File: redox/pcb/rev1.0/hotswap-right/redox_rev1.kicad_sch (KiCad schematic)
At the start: 75 parts, among them K0 KEYSW, K1 KEYSW, K10 KEYSW, K11 KEYSW, K12 KEYSW, K13 KEYSW, K14 KEYSW, K15 KEYSW, K16 KEYSW, K2 KEYSW, K20 KEYSW, K21 KEYSW, K22 KEYSW, K23 KEYSW, K24 KEYSW, K25 KEYSW, K26 KEYSW, K3 KEYSW, K30 KEYSW, K31 KEYSW, K32 KEYSW, K33 KEYSW, K34 KEYSW, K35 KEYSW, K36 KEYSW, K4 KEYSW, K40 KEYSW, K41 KEYSW, K42 KEYSW, K43 KEYSW, K44 KEYSW, K45 KEYSW, K46 KEYSW, K5 KEYSW, K6 KEYSW, U1 ProMicro

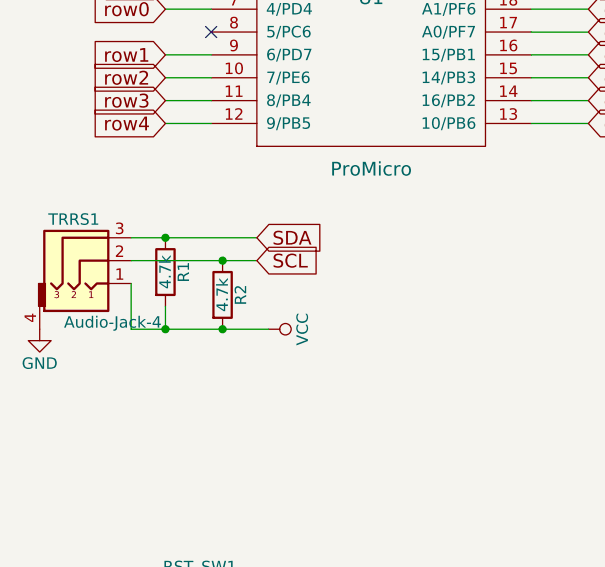
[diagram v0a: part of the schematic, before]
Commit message: Remove pullup resistors from right schematic
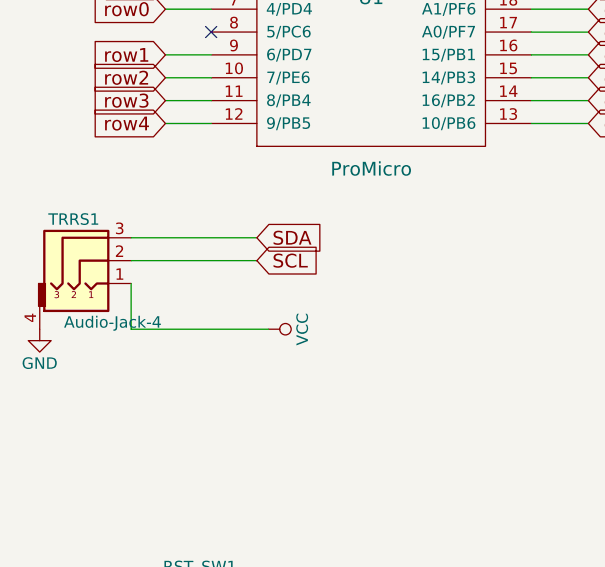
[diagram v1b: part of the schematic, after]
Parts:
- removed R1, R2: 4.7k, redox_footprints:Resistor-Compact, symbol redox_rev1-rescue:R
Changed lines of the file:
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@@
   (junction (at 177.8 48.26) (diameter 0) (color 0 0 0 0)
   )
-  (junction (at 43.18 83.82) (diameter 0) (color 0 0 0 0)
-  )
   (junction (at 233.68 57.15) (diameter 0) (color 0 0 0 0)
   )
@@
   (junction (at 152.4 74.93) (diameter 0) (color 0 0 0 0)
   )
-  (junction (at 36.83 91.44) (diameter 0) (color 0 0 0 0)
-  )
   (junction (at 157.48 124.46) (diameter 0) (color 0 0 0 0)
   )
@@
   (junction (at 137.16 124.46) (diameter 0) (color 0 0 0 0)
   )
-  (junction (at 36.83 81.28) (diameter 0) (color 0 0 0 0)
-  )
   (junction (at 218.44 104.14) (diameter 0) (color 0 0 0 0)
   )
@@
   )
   (junction (at 198.12 104.14) (diameter 0) (color 0 0 0 0)
-  )
-  (junction (at 43.18 91.44) (diameter 0) (color 0 0 0 0)
   )
   (junction (at 218.44 48.26) (diameter 0) (color 0 0 0 0)
@@
     (stroke (width 0) (type default) (color 0 0 0 0))
   )
-  (wire (pts (xy 36.83 81.28) (xy 46.99 81.28))
-    (stroke (width 0) (type default) (color 0 0 0 0))
-  )
-  (wire (pts (xy 36.83 91.44) (xy 43.18 91.44))
+  (wire (pts (xy 33.02 81.28) (xy 46.99 81.28))
     (stroke (width 0) (type default) (color 0 0 0 0))
   )
@@
     (stroke (width 0) (type default) (color 0 0 0 0))
   )
-  (wire (pts (xy 43.18 91.44) (xy 48.26 91.44))
+  (wire (pts (xy 33.02 91.44) (xy 48.26 91.44))
     (stroke (width 0) (type default) (color 0 0 0 0))
   )
@@
     (stroke (width 0) (type default) (color 0 0 0 0))
   )
-  (wire (pts (xy 33.02 81.28) (xy 36.83 81.28))
-    (stroke (width 0) (type default) (color 0 0 0 0))
-  )
   (wire (pts (xy 157.48 74.93) (xy 157.48 77.47))
     (stroke (width 0) (type default) (color 0 0 0 0))
@@
     (stroke (width 0) (type default) (color 0 0 0 0))
   )
-  (wire (pts (xy 36.83 88.9) (xy 36.83 91.44))
-    (stroke (width 0) (type default) (color 0 0 0 0))
-  )
   (wire (pts (xy 198.12 114.3) (xy 198.12 116.84))
     (stroke (width 0) (type default) (color 0 0 0 0))
@@
     (stroke (width 0) (type default) (color 0 0 0 0))
   )
-  (wire (pts (xy 43.18 83.82) (xy 46.99 83.82))
+  (wire (pts (xy 33.02 83.82) (xy 46.99 83.82))
     (stroke (width 0) (type default) (color 0 0 0 0))
   )
@@
     (stroke (width 0) (type default) (color 0 0 0 0))
   )
-  (wire (pts (xy 33.02 91.44) (xy 36.83 91.44))
-    (stroke (width 0) (type default) (color 0 0 0 0))
-  )
   (wire (pts (xy 218.44 38.1) (xy 218.44 40.64))
     (stroke (width 0) (type default) (color 0 0 0 0))
@@
   )
   (wire (pts (xy 198.12 104.14) (xy 218.44 104.14))
-    (stroke (width 0) (type default) (color 0 0 0 0))
-  )
-  (wire (pts (xy 33.02 83.82) (xy 43.18 83.82))
     (stroke (width 0) (type default) (color 0 0 0 0))
   )
@@
     (pin "2")
   )
-  (symbol (lib_id "redox_rev1-rescue:R") (at 36.83 85.09 0) (unit 1)
-    (in_bom yes) (on_board yes)
-    (property "Reference" "R1" (id 0) (at 38.862 85.09 90))
-    (property "Value" "4.7k" (id 1) (at 36.83 85.09 90))
-    (property "Footprint" "redox_footprints:Resistor-Compact" (id 2) (at 35.052 85.09 90)
-      (effects (font (size 1.27 1.27)) hide)
-    )
-    (property "Datasheet" "" (id 3) (at 36.83 85.09 0)
-      (effects (font (size 1.27 1.27)) hide)
-    )
-    (pin "1")
-    (pin "2")
-  )
-  (symbol (lib_id "redox_rev1-rescue:R") (at 43.18 87.63 0) (unit 1)
-    (in_bom yes) (on_board yes)
-    (property "Reference" "R2" (id 0) (at 45.212 87.63 90))
-    (property "Value" "4.7k" (id 1) (at 43.18 87.63 90))
-    (property "Footprint" "redox_footprints:Resistor-Compact" (id 2) (at 41.402 87.63 90)
-      (effects (font (size 1.27 1.27)) hide)
-    )
-    (property "Datasheet" "" (id 3) (at 43.18 87.63 0)
-      (effects (font (size 1.27 1.27)) hide)
-    )
-    (pin "1")
-    (pin "2")
-  )
   (symbol (lib_id "redox_rev1-rescue:KEYSW") (at 124.46 74.93 0) (unit 1)
     (in_bom yes) (on_board yes)
@@
       (reference "K46") (unit 1) (value "KEYSW") (footprint "redox_footprints:Kailh_socket_MX")
     )
-    (path "/00000000-0000-0000-0000-00005a80a2df"
-      (reference "R1") (unit 1) (value "4.7k") (footprint "redox_footprints:Resistor-Compact")
-    )
-    (path "/00000000-0000-0000-0000-00005a80a522"
-      (reference "R2") (unit 1) (value "4.7k") (footprint "redox_footprints:Resistor-Compact")
-    )
     (path "/00000000-0000-0000-0000-00005a808917"
